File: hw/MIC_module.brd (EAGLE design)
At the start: 25 x 45 mm, 39 parts, among them J1 GROVE-4P-2.0-3470130P1, J2 GROVE-4P-2.0-3470130P1

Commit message: layout completed
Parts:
- removed J3: (no value), OPL-Connector:9+4P-SMD-L16.1*W14.5*H1.85MM
- removed R6, R7, R9: 100k, rcl:R0603
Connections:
- removed net SD_!CD: J3.9
- removed net SD_!CS: J3.2, R9.1
- removed net SD_CLK: J3.5
- removed net SD_MISO: J3.7, R6.1
- removed net SD_MOSI: J3.3, R7.1
- net +3V3: no longer J3.4, R6.2, R7.2, R9.2
- net GND: no longer J3.6
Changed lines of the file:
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@@
 <element name="R5" library="rcl" package="R0603" value="100" x="18.7" y="23.2" rot="R270"/>
 <element name="C15" library="rcl" package="C0603" value="15p" x="17.3" y="23.2" rot="R270"/>
-<element name="J3" library="OPL-Connector" package="9+4P-SMD-L16.1*W14.5*H1.85MM" value="" x="-3.5" y="-11.5"/>
-<element name="R6" library="rcl" package="R0603" value="100k" x="-3" y="-22.5"/>
-<element name="R7" library="rcl" package="R0603" value="100k" x="2.5" y="-22.5"/>
-<element name="R9" library="rcl" package="R0603" value="100k" x="8" y="-22.5"/>
 </elements>
 <signals>
@@
 <via x="23.4" y="44.1" extent="1-16" drill="0.3"/>
 <via x="24.1" y="43.4" extent="1-16" drill="0.3"/>
-<contactref element="J3" pad="6"/>
-<wire x1="24.1" y1="43.4" x2="23.4" y2="44.1" width="0" layer="19" extent="1-1"/>
-<wire x1="19" y1="40.65" x2="23.4" y2="44.1" width="0" layer="19" extent="1-1"/>
-<wire x1="16.8" y1="41.5" x2="19" y2="40.65" width="0" layer="19" extent="1-1"/>
-<wire x1="15" y1="42.8" x2="16.8" y2="41.5" width="0" layer="19" extent="1-1"/>
-<wire x1="13.2" y1="41.5" x2="15" y2="42.8" width="0" layer="19" extent="1-1"/>
-<wire x1="11.8" y1="41.5" x2="13.2" y2="41.5" width="0" layer="19" extent="1-1"/>
-<wire x1="15" y1="40.2" x2="16.8" y2="41.5" width="0" layer="19" extent="1-1"/>
-<wire x1="15" y1="38.8" x2="15" y2="40.2" width="0" layer="19" extent="1-1"/>
-<wire x1="16.8" y1="37.5" x2="15" y2="38.8" width="0" layer="19" extent="1-1"/>
-<wire x1="10" y1="42.8" x2="11.8" y2="41.5" width="0" layer="19" extent="1-1"/>
-<wire x1="8.2" y1="41.5" x2="10" y2="42.8" width="0" layer="19" extent="1-1"/>
-<wire x1="15" y1="36.2" x2="16.8" y2="37.5" width="0" layer="19" extent="1-1"/>
-<wire x1="13.2" y1="37.5" x2="15" y2="38.8" width="0" layer="19" extent="1-1"/>
-<wire x1="11.8" y1="37.5" x2="13.2" y2="37.5" width="0" layer="19" extent="1-1"/>
-<wire x1="10" y1="40.2" x2="11.8" y2="41.5" width="0" layer="19" extent="1-1"/>
-<wire x1="10" y1="38.8" x2="10" y2="40.2" width="0" layer="19" extent="1-1"/>
-<wire x1="8.2" y1="37.5" x2="10" y2="38.8" width="0" layer="19" extent="1-1"/>
-<wire x1="10" y1="36.2" x2="11.8" y2="37.5" width="0" layer="19" extent="1-1"/>
-<wire x1="9.65" y1="34" x2="10" y2="36.2" width="0" layer="19" extent="1-1"/>
-<wire x1="19" y1="36.65" x2="16.8" y2="37.5" width="0" layer="19" extent="1-1"/>
-<wire x1="6" y1="42.35" x2="8.2" y2="41.5" width="0" layer="19" extent="1-1"/>
-<wire x1="6" y1="38.35" x2="8.2" y2="37.5" width="0" layer="19" extent="1-1"/>
-<wire x1="1.6" y1="44.1" x2="6" y2="42.35" width="0" layer="19" extent="1-1"/>
-<wire x1="0.9" y1="43.4" x2="1.6" y2="44.1" width="0" layer="19" extent="1-1"/>
-<wire x1="8.65" y1="20.9" x2="9.65" y2="34" width="0" layer="19" extent="1-1"/>
-<wire x1="12.55" y1="20.75" x2="8.65" y2="20.9" width="0" layer="19" extent="1-1"/>
-<wire x1="17.3" y1="22.35" x2="12.55" y2="20.75" width="0" layer="19" extent="1-1"/>
-<wire x1="17.7" y1="17.4" x2="17.3" y2="22.35" width="0" layer="19" extent="1-1"/>
-<wire x1="19.05" y1="17.25" x2="17.7" y2="17.4" width="0" layer="19" extent="1-1"/>
-<wire x1="21.875" y1="16.7625" x2="19.05" y2="17.25" width="0" layer="19" extent="1-1"/>
-<wire x1="21.85" y1="18" x2="21.875" y2="16.7625" width="0" layer="19" extent="1-1"/>
-<wire x1="23.55" y1="19.4" x2="21.85" y2="18" width="0" layer="19" extent="1-1"/>
-<wire x1="17.05" y1="12.25" x2="17.7" y2="17.4" width="0" layer="19" extent="1-1"/>
-<wire x1="19.2" y1="10.35" x2="17.05" y2="12.25" width="0" layer="19" extent="1-1"/>
-<wire x1="20.9" y1="10.35" x2="19.2" y2="10.35" width="0" layer="19" extent="1-1"/>
-<wire x1="20.225" y1="8.925" x2="20.9" y2="10.35" width="0" layer="19" extent="1-1"/>
-<wire x1="19.9" y1="7.7" x2="20.225" y2="8.925" width="0" layer="19" extent="1-1"/>
-<wire x1="20.875" y1="6.475" x2="19.9" y2="7.7" width="0" layer="19" extent="1-1"/>
-<wire x1="17.3" y1="6.85" x2="19.9" y2="7.7" width="0" layer="19" extent="1-1"/>
-<wire x1="17.3" y1="5.9" x2="17.3" y2="6.85" width="0" layer="19" extent="1-1"/>
-<wire x1="15.9" y1="6.85" x2="17.3" y2="6.85" width="0" layer="19" extent="1-1"/>
-<wire x1="15.9" y1="5.9" x2="15.9" y2="6.85" width="0" layer="19" extent="1-1"/>
-<wire x1="14.5" y1="8.55" x2="15.9" y2="6.85" width="0" layer="19" extent="1-1"/>
-<wire x1="16" y1="3.2" x2="15.9" y2="5.9" width="0" layer="19" extent="1-1"/>
-<wire x1="12.5" y1="2.75" x2="16" y2="3.2" width="0" layer="19" extent="1-1"/>
-<wire x1="24.1" y1="1.6" x2="20.875" y2="6.475" width="0" layer="19" extent="1-1"/>
-<wire x1="23.4" y1="0.9" x2="24.1" y2="1.6" width="0" layer="19" extent="1-1"/>
-<wire x1="8.1" y1="8.2" x2="14.5" y2="8.55" width="0" layer="19" extent="1-1"/>
-<wire x1="7.1" y1="8.2" x2="8.1" y2="8.2" width="0" layer="19" extent="1-1"/>
-<wire x1="7.1" y1="7.7" x2="7.1" y2="8.2" width="0" layer="19" extent="1-1"/>
-<wire x1="7.1" y1="7.2" x2="7.1" y2="7.7" width="0" layer="19" extent="1-1"/>
-<wire x1="6.1" y1="8.7" x2="7.1" y2="8.2" width="0" layer="19" extent="1-1"/>
-<wire x1="4.5" y1="8.9" x2="6.1" y2="8.7" width="0" layer="19" extent="1-1"/>
-<wire x1="3.7" y1="8.9" x2="4.5" y2="8.9" width="0" layer="19" extent="1-1"/>
-<wire x1="4.1" y1="10.3" x2="4.5" y2="8.9" width="0" layer="19" extent="1-1"/>
-<wire x1="6.15" y1="10.4" x2="6.1" y2="8.7" width="0" layer="19" extent="1-1"/>
-<wire x1="6.55" y1="12.1" x2="6.15" y2="10.4" width="0" layer="19" extent="1-1"/>
-<wire x1="8.65" y1="12.1" x2="6.55" y2="12.1" width="0" layer="19" extent="1-1"/>
-<wire x1="10.55" y1="14.25" x2="8.65" y2="12.1" width="0" layer="19" extent="1-1"/>
-<wire x1="1.7" y1="14.26" x2="4.1" y2="10.3" width="0" layer="19" extent="1-1"/>
-<wire x1="1.7" y1="15.53" x2="1.7" y2="14.26" width="0" layer="19" extent="1-1"/>
-<wire x1="1.7" y1="16.8" x2="1.7" y2="15.53" width="0" layer="19" extent="1-1"/>
-<wire x1="1.7" y1="18.07" x2="1.7" y2="16.8" width="0" layer="19" extent="1-1"/>
-<wire x1="3" y1="3.2" x2="7.1" y2="7.2" width="0" layer="19" extent="1-1"/>
-<wire x1="0.9" y1="1.6" x2="3" y2="3.2" width="0" layer="19" extent="1-1"/>
-<wire x1="1.6" y1="0.9" x2="0.9" y2="1.6" width="0" layer="19" extent="1-1"/>
-<wire x1="-3.5" y1="-14.75" x2="1.6" y2="0.9" width="0" layer="19" extent="1-1"/>
 </signal>
 <signal name="VIN">
@@
 <via x="18" y="34.5" extent="1-16" drill="0.3"/>
 <wire x1="18" y1="34.5" x2="18" y2="38.5" width="0.6" layer="16"/>
-<contactref element="J3" pad="4"/>
-<contactref element="R9" pad="2"/>
-<contactref element="R7" pad="2"/>
-<contactref element="R6" pad="2"/>
-<wire x1="11.2" y1="10.55" x2="13" y2="10" width="0" layer="19" extent="1-1"/>
-<wire x1="8.05" y1="10.75" x2="10.35" y2="12.1" width="0" layer="19" extent="1-1"/>
-<wire x1="8.05" y1="10.4" x2="8.05" y2="10.55" width="0" layer="19" extent="1-1"/>
-<wire x1="-3.5" y1="-12.55" x2="6.1" y2="6.1" width="0" layer="19" extent="1-1"/>
-<wire x1="-2.15" y1="-22.5" x2="-3.5" y2="-12.55" width="0" layer="19" extent="1-1"/>
-<wire x1="3.35" y1="-22.5" x2="-2.15" y2="-22.5" width="0" layer="19" extent="1-1"/>
-<wire x1="8.85" y1="-22.5" x2="3.35" y2="-22.5" width="0" layer="19" extent="1-1"/>
 </signal>
 <signal name="JTMS">
@@
 <wire x1="16.05" y1="20.75" x2="16.05" y2="19.55" width="0.2" layer="1"/>
 </signal>
-<signal name="SD_!CS">
-<contactref element="J3" pad="2"/>
-<contactref element="R9" pad="1"/>
-<wire x1="-3.5" y1="-10.35" x2="7.15" y2="-22.5" width="0" layer="19" extent="1-1"/>
-</signal>
-<signal name="SD_CLK">
-<contactref element="J3" pad="5"/>
-</signal>
-<signal name="SD_MOSI">
-<contactref element="J3" pad="3"/>
-<contactref element="R7" pad="1"/>
-<wire x1="-3.5" y1="-11.45" x2="1.65" y2="-22.5" width="0" layer="19" extent="1-1"/>
-</signal>
-<signal name="SD_MISO">
-<contactref element="J3" pad="7"/>
-<contactref element="R6" pad="1"/>
-<wire x1="-3.5" y1="-15.85" x2="-3.85" y2="-22.5" width="0" layer="19" extent="1-1"/>
-</signal>
-<signal name="SD_!CD">
-<contactref element="J3" pad="9"/>
-</signal>
 </signals>

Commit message: layout in progress
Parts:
- removed U$6: STM32F303C, st:LQFP48
- added C16, C18: 2u2, rcl:C0603
- added IC1: STM32F405RGT, micro-stm_v2:LQFP64
- moved C17 11.0 mm to (16.5, 28.5), turned to 90 degrees
- moved C14 7.60 mm to (9.40, 28.5), turned to 90 degrees
- moved C15 5.36 mm to (18.1, 28.5)
- moved R5 5.36 mm to (19.5, 28.5)
- moved C6 2.10 mm to (22.7, 20.1)
- moved U$5 2.10 mm to (22.7, 18.1)
- moved R1 1.13 mm to (23.5, 14.8), turned to 90 degrees
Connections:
- removed net MIC_CLK_X2: U$6.15, U$6.16, U$6.26
- new net N$6: C16.2, IC1.47
- new net N$9: C18.2, IC1.31
- net +3V3: now also IC1.1, IC1.13, IC1.19, IC1.32, IC1.48, IC1.64; no longer U$6.1, U$6.24, U$6.36, U$6.48, U$6.9
- net BOOT0: now also IC1.60; no longer U$6.44
- net CAN_RX: now also IC1.61; no longer U$6.45
- net CAN_TX: now also IC1.62; no longer U$6.46
- net GND: now also C16.1, C18.1, IC1.12, IC1.18, IC1.63; no longer U$6.23, U$6.35, U$6.47, U$6.8
- net JTCK: now also IC1.49; no longer U$6.37
- net JTDI: now also IC1.50; no longer U$6.38
- net JTDO: now also IC1.55; no longer U$6.39
- net JTMS: now also IC1.46; no longer U$6.34
- net LED1: no longer U$6.2
- net MIC_CLK_UC: no longer U$6.12
- net MIC_PDM12: no longer U$6.28
- net MIC_PDM34: no longer U$6.17
- net NRST: now also IC1.7; no longer U$6.7
- net OSC_IN: now also IC1.5; no longer U$6.5
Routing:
- net +3V3: track 148.2 -> 133.6 mm, vias 14 -> 12
- net MIC_CLK_X2: track 7.53 -> 0.00 mm
- net MIC_CLK: track 30.8 -> 23.6 mm
- net MIC_PDM12: track 43.6 -> 37.1 mm, vias 3 -> 2
- net LED1: track 2.90 -> 0.00 mm
- net N$9: track 0.00 -> 2.49 mm
- net MIC_CLK_UC: track 3.24 -> 1.34 mm
- net N$6: track 0.00 -> 1.76 mm
- net CAN_TX: track 7.66 -> 9.26 mm
- net CAN_RX: track 4.78 -> 6.38 mm
- net BOOT0: track 3.84 -> 5.44 mm
- net MIC_PDM34: track 37.8 -> 36.3 mm, vias 3 -> 2
- net JTDO: track 13.4 -> 14.8 mm

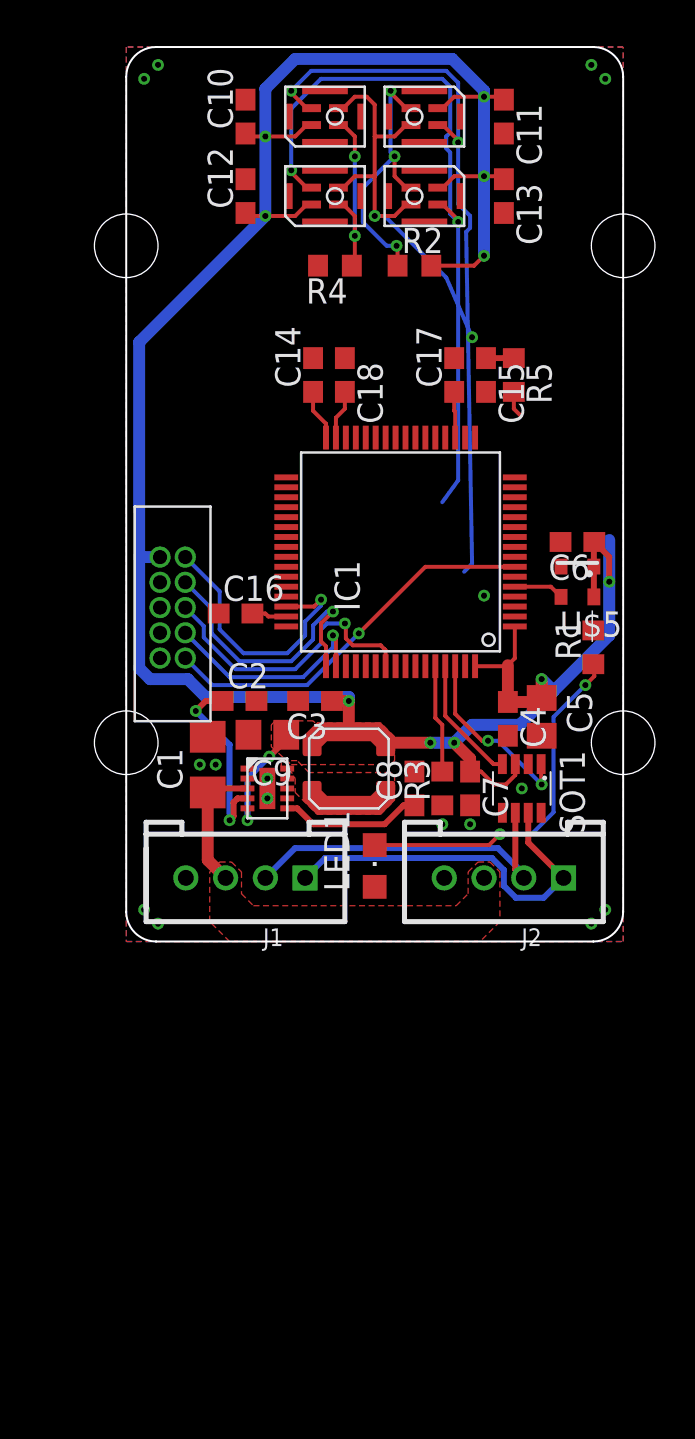
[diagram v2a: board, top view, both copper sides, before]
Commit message: added USB port
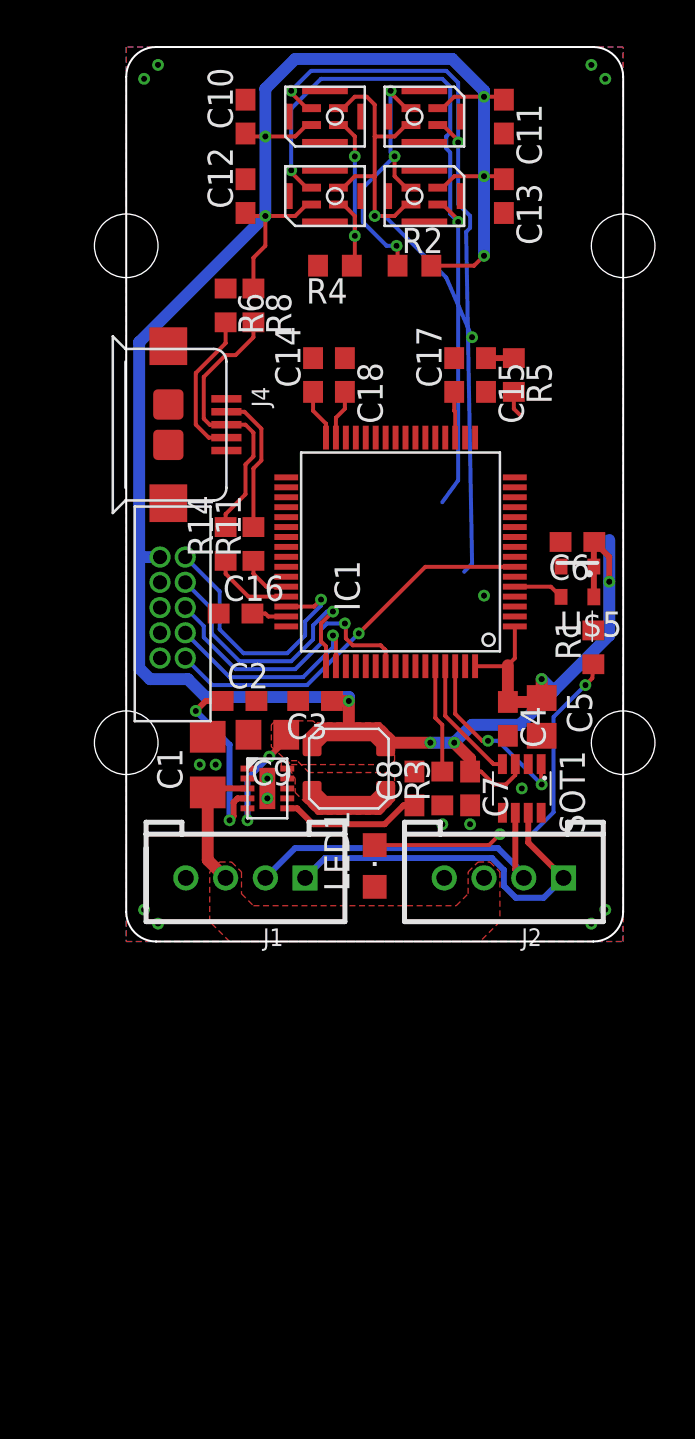
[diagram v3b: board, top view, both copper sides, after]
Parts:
- added J4: MICRO-USB-5P-340015001, OPL Eagle Library:B-SMD-5P
- added R11, R14: 22, rcl:R0603
- added R6: 100k, rcl:R0603
- added R8: 1k5, rcl:R0603
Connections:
- new net N$3: J4.2, R11.2
- new net N$32: J4.3, R14.2, R8.2
- new net N$5: J4.4, R6.2
- new net USB_N: IC1.44, R11.1
- new net USB_P: IC1.45, R14.1
- new net USB_VBUS: J4.1
- net +3V3: now also R8.1
- net GND: now also J4.5, J4.E1, J4.E2, J4.P1, J4.P2, R6.1
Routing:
- net N$32: track 0.00 -> 14.3 mm
- net N$5: track 0.00 -> 7.58 mm
- net N$3: track 0.00 -> 7.23 mm
- net USB_P: track 0.00 -> 4.18 mm
- net +3V3: track 133.6 -> 137.5 mm
- net USB_N: track 0.00 -> 2.57 mm
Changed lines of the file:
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@@
 <layer number="42" name="bRestrict" color="1" fill="10" visible="no" active="yes"/>
 <layer number="43" name="vRestrict" color="2" fill="10" visible="no" active="yes"/>
-<layer number="44" name="Drills" color="7" fill="1" visible="no" active="yes"/>
+<layer number="44" name="Drills" color="7" fill="1" visible="yes" active="yes"/>
 <layer number="45" name="Holes" color="7" fill="1" visible="yes" active="yes"/>
 <layer number="46" name="Milling" color="3" fill="1" visible="yes" active="yes"/>
-<layer number="47" name="Measures" color="7" fill="1" visible="no" active="yes"/>
+<layer number="47" name="Measures" color="7" fill="1" visible="yes" active="yes"/>
 <layer number="48" name="Document" color="7" fill="1" visible="yes" active="yes"/>
 <layer number="49" name="Reference" color="7" fill="1" visible="no" active="yes"/>
 <layer number="50" name="dxf" color="7" fill="1" visible="no" active="no"/>
-<layer number="51" name="tDocu" color="7" fill="1" visible="yes" active="yes"/>
+<layer number="51" name="tDocu" color="7" fill="1" visible="no" active="yes"/>
 <layer number="52" name="bDocu" color="7" fill="1" visible="no" active="yes"/>
 <layer number="53" name="tGND_GNDA" color="7" fill="1" visible="no" active="no"/>
@@
 <element name="C16" library="rcl" package="C0603" value="2u2" x="5.5" y="16.5"/>
 <element name="C18" library="rcl" package="C0603" value="2u2" x="11" y="28.5" rot="R270"/>
+<element name="R11" library="rcl" package="R0603" value="22" x="6.4" y="20" rot="R90"/>
+<element name="R14" library="rcl" package="R0603" value="22" x="5" y="20" rot="R90"/>
+<element name="R6" library="rcl" package="R0603" value="100k" x="5" y="32" rot="R270"/>
+<element name="R8" library="rcl" package="R0603" value="1k5" x="6.4" y="32" rot="R270"/>
+<element name="J4" library="OPL Eagle Library" package="B-SMD-5P" value="MICRO-USB-5P-340015001" x="2.5" y="26" rot="R270"/>
 </elements>
 <signals>
@@
 <contactref element="C16" pad="1"/>
 <contactref element="C18" pad="1"/>
+<contactref element="J4" pad="5"/>
+<contactref element="J4" pad="E2"/>
+<contactref element="J4" pad="E1"/>
+<contactref element="J4" pad="P2"/>
+<contactref element="J4" pad="P1"/>
+<contactref element="R6" pad="1"/>
 </signal>
 <signal name="VIN">
@@
 <wire x1="24.3" y1="18.1" x2="24.3" y2="20.2" width="0.6" layer="16"/>
 <wire x1="0.65" y1="13.75" x2="0.65" y2="19.34" width="0.6" layer="16"/>
-<wire x1="0.65" y1="19.34" x2="0.65" y2="21.7" width="0.6" layer="16"/>
 <wire x1="1.7" y1="19.34" x2="0.65" y2="19.34" width="0.6" layer="16"/>
 <contactref element="U$5" pad="4"/>
@@
 <wire x1="7" y1="40.5" x2="7" y2="36.5" width="0.6" layer="16"/>
 <wire x1="7" y1="36.5" x2="0.65" y2="30.15" width="0.6" layer="16"/>
-<wire x1="0.65" y1="30.15" x2="0.65" y2="21.7" width="0.6" layer="16"/>
+<wire x1="0.65" y1="30.15" x2="0.65" y2="19.34" width="0.6" layer="16"/>
 <wire x1="15.35" y1="34" x2="17.5" y2="34" width="0.2" layer="1"/>
 <wire x1="17.5" y1="34" x2="18" y2="34.5" width="0.2" layer="1"/>
@@
 <wire x1="16.5" y1="26.7" x2="16.5" y2="27.65" width="0.2" layer="1"/>
 <wire x1="10.35" y1="12.1" x2="11.2" y2="12.1" width="0.6" layer="1"/>
+<contactref element="R8" pad="1"/>
+<wire x1="6.4" y1="32.85" x2="6.4" y2="34.4" width="0.2" layer="1"/>
+<wire x1="6.4" y1="34.4" x2="7" y2="35" width="0.2" layer="1"/>
+<wire x1="7" y1="35" x2="7" y2="36.5" width="0.2" layer="1"/>
 <wire x1="23.525" y1="20.075" x2="19.55" y2="21.85" width="0" layer="19" extent="1-1"/>
 <wire x1="8.05" y1="15.85" x2="10.35" y2="12.1" width="0" layer="19" extent="1-1"/>
 <wire x1="16.55" y1="25.35" x2="19.55" y2="21.85" width="0" layer="19" extent="1-1"/>
-<wire x1="10.05" y1="26.05" x2="16.5" y2="26.7" width="0" layer="19" extent="1-1"/>
+<wire x1="9.4" y1="27.65" x2="6.4" y2="32.85" width="0" layer="19" extent="1-1"/>
 </signal>
 <signal name="JTMS">
@@
 <contactref element="LED1" pad="C"/>
 <via x="23.1" y="12.9" extent="1-16" drill="0.3"/>
-<wire x1="23.5" y1="13.95" x2="23.55" y2="13.35" width="0.2" layer="1"/>
-<wire x1="23.55" y1="13.35" x2="23.1" y2="12.9" width="0.2" layer="1"/>
+<wire x1="23.5" y1="13.95" x2="23.45" y2="13.25" width="0.2" layer="1"/>
+<wire x1="23.45" y1="13.25" x2="23.1" y2="12.9" width="0.2" layer="1"/>
 <wire x1="12.5" y1="4.85" x2="18.25" y2="4.85" width="0.2" layer="1"/>
 <wire x1="18.25" y1="4.85" x2="18.8" y2="5.4" width="0.2" layer="1"/>
@@
 <wire x1="11" y1="26.8" x2="11" y2="27.65" width="0.2" layer="1"/>
 </signal>
+<signal name="USB_VBUS">
+<contactref element="J4" pad="1"/>
+</signal>
+<signal name="USB_N">
+<contactref element="R11" pad="1"/>
+<contactref element="IC1" pad="44"/>
+<wire x1="8.05" y1="17.85" x2="7.05" y2="17.85" width="0.2" layer="1"/>
+<wire x1="7.05" y1="17.85" x2="6.4" y2="18.5" width="0.2" layer="1"/>
+<wire x1="6.4" y1="18.5" x2="6.4" y2="19.15" width="0.2" layer="1"/>
+</signal>
+<signal name="USB_P">
+<contactref element="R14" pad="1"/>
+<contactref element="IC1" pad="45"/>
+<wire x1="8.05" y1="17.35" x2="6.15" y2="17.35" width="0.2" layer="1"/>
+<wire x1="6.15" y1="17.35" x2="5" y2="18.5" width="0.2" layer="1"/>
+<wire x1="5" y1="18.5" x2="5" y2="19.15" width="0.2" layer="1"/>
+</signal>
+<signal name="N$3">
+<contactref element="R11" pad="2"/>
+<contactref element="J4" pad="2"/>
+<wire x1="6.4" y1="20.85" x2="6.4" y2="23.8" width="0.2" layer="1"/>
+<wire x1="6.4" y1="23.8" x2="6.8" y2="24.2" width="0.2" layer="1"/>
+<wire x1="6.8" y1="24.2" x2="6.8" y2="25.8" width="0.2" layer="1"/>
+<wire x1="6.8" y1="25.8" x2="5.95" y2="26.65" width="0.2" layer="1"/>
+<wire x1="5.04" y1="26.65" x2="5.95" y2="26.65" width="0.2" layer="1"/>
+</signal>
+<signal name="N$32">
+<contactref element="R14" pad="2"/>
+<contactref element="R8" pad="2"/>
+<contactref element="J4" pad="3"/>
+<wire x1="6.4" y1="24.4" x2="6.4" y2="25.6" width="0.2" layer="1"/>
+<wire x1="6.4" y1="25.6" x2="6" y2="26" width="0.2" layer="1"/>
+<wire x1="6" y1="26" x2="5.04" y2="26" width="0.2" layer="1"/>
+<wire x1="6.4" y1="24.4" x2="6" y2="24" width="0.2" layer="1"/>
+<wire x1="6" y1="24" x2="6" y2="22.5" width="0.2" layer="1"/>
+<wire x1="6" y1="22.5" x2="5" y2="21.5" width="0.2" layer="1"/>
+<wire x1="5" y1="21.5" x2="5" y2="20.85" width="0.2" layer="1"/>
+<wire x1="6.4" y1="31.15" x2="6.4" y2="30.4" width="0.2" layer="1"/>
+<wire x1="6.4" y1="30.4" x2="5.5" y2="29.5" width="0.2" layer="1"/>
+<wire x1="5.5" y1="29.5" x2="5" y2="29.5" width="0.2" layer="1"/>
+<wire x1="5" y1="29.5" x2="3.9" y2="28.4" width="0.2" layer="1"/>
+<wire x1="3.9" y1="28.4" x2="3.9" y2="26.3" width="0.2" layer="1"/>
+<wire x1="3.9" y1="26.3" x2="4.2" y2="26" width="0.2" layer="1"/>
+<wire x1="4.2" y1="26" x2="5.04" y2="26" width="0.2" layer="1"/>
+</signal>
+<signal name="N$5">
+<contactref element="R6" pad="2"/>
+<contactref element="J4" pad="4"/>
+<wire x1="5" y1="31.15" x2="5" y2="30.1" width="0.2" layer="1"/>
+<wire x1="5" y1="30.1" x2="3.5" y2="28.6" width="0.2" layer="1"/>
+<wire x1="3.5" y1="28.6" x2="3.5" y2="26" width="0.2" layer="1"/>
+<wire x1="3.5" y1="26" x2="4.15" y2="25.35" width="0.2" layer="1"/>
+<wire x1="5.04" y1="25.35" x2="4.15" y2="25.35" width="0.2" layer="1"/>
+</signal>
 </signals>
